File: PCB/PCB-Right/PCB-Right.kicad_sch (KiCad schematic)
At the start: 56 parts, among them J1 USB_C_Receptacle_USB2.0_16P, J2 Conn_ARM_JTAG_SWD_10, Q1 2N7002, SW1 SW_RST, SW2 SW_SPDT, U2 XC6206PxxxMR, U3 SRV05-4, U4 BQ24075RGT, U5 MDBT50Q-1MV2, Y1 32.768KHz

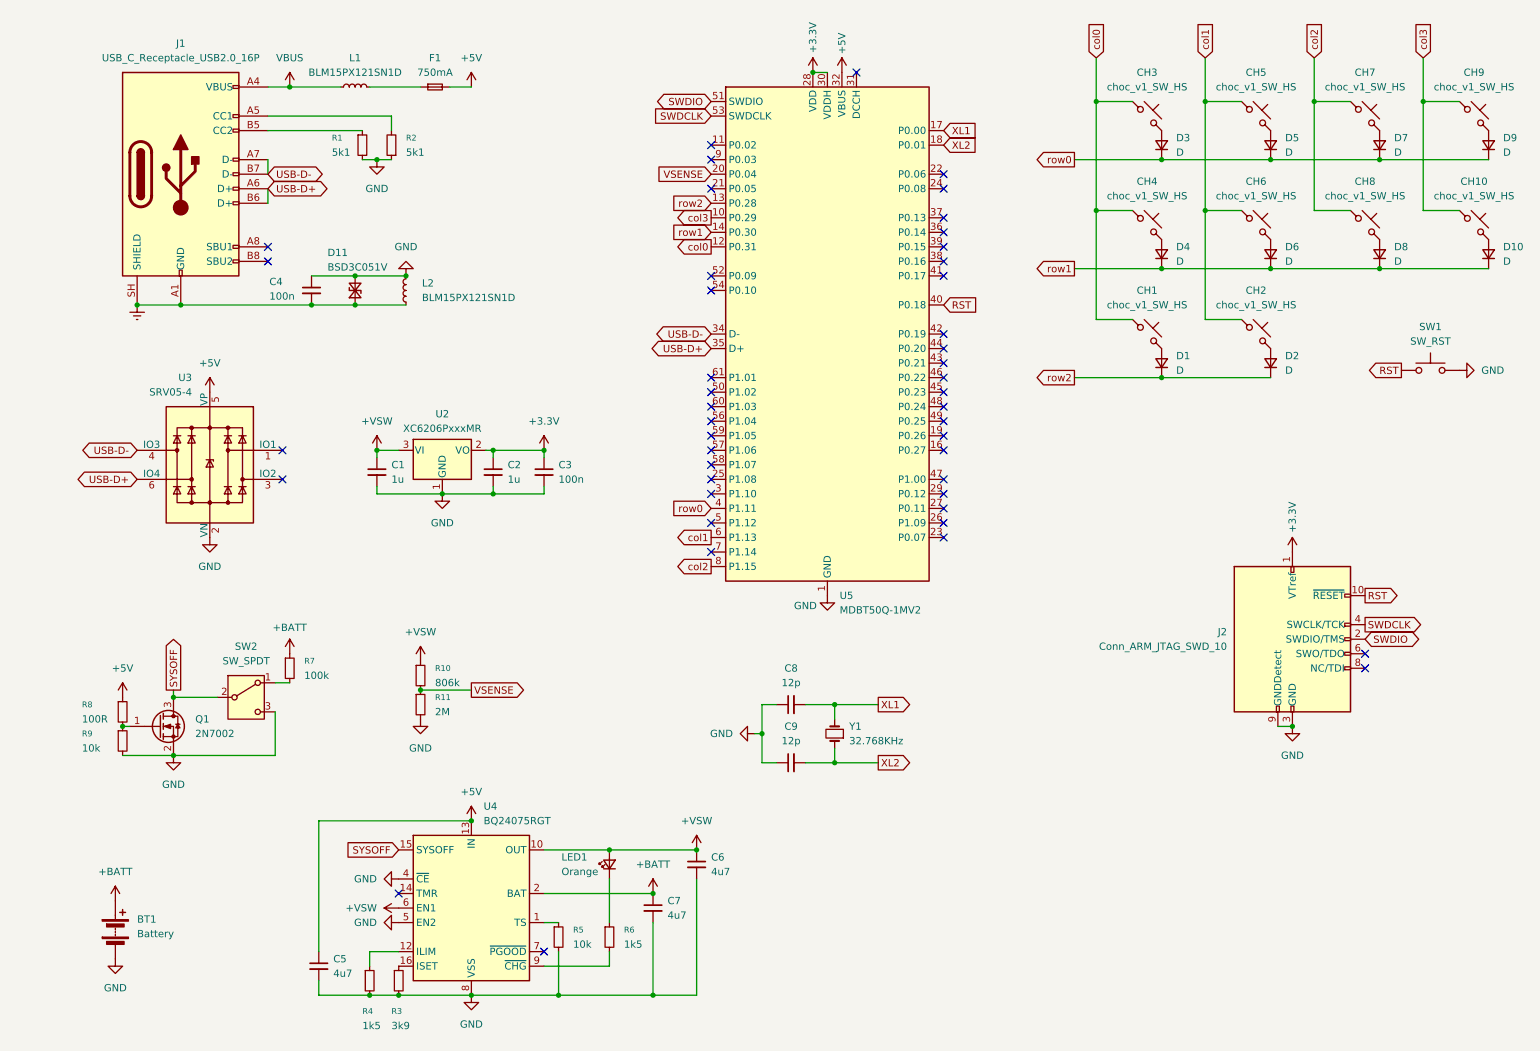
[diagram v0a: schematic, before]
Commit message: replace voltage regulator with DCCH inductor
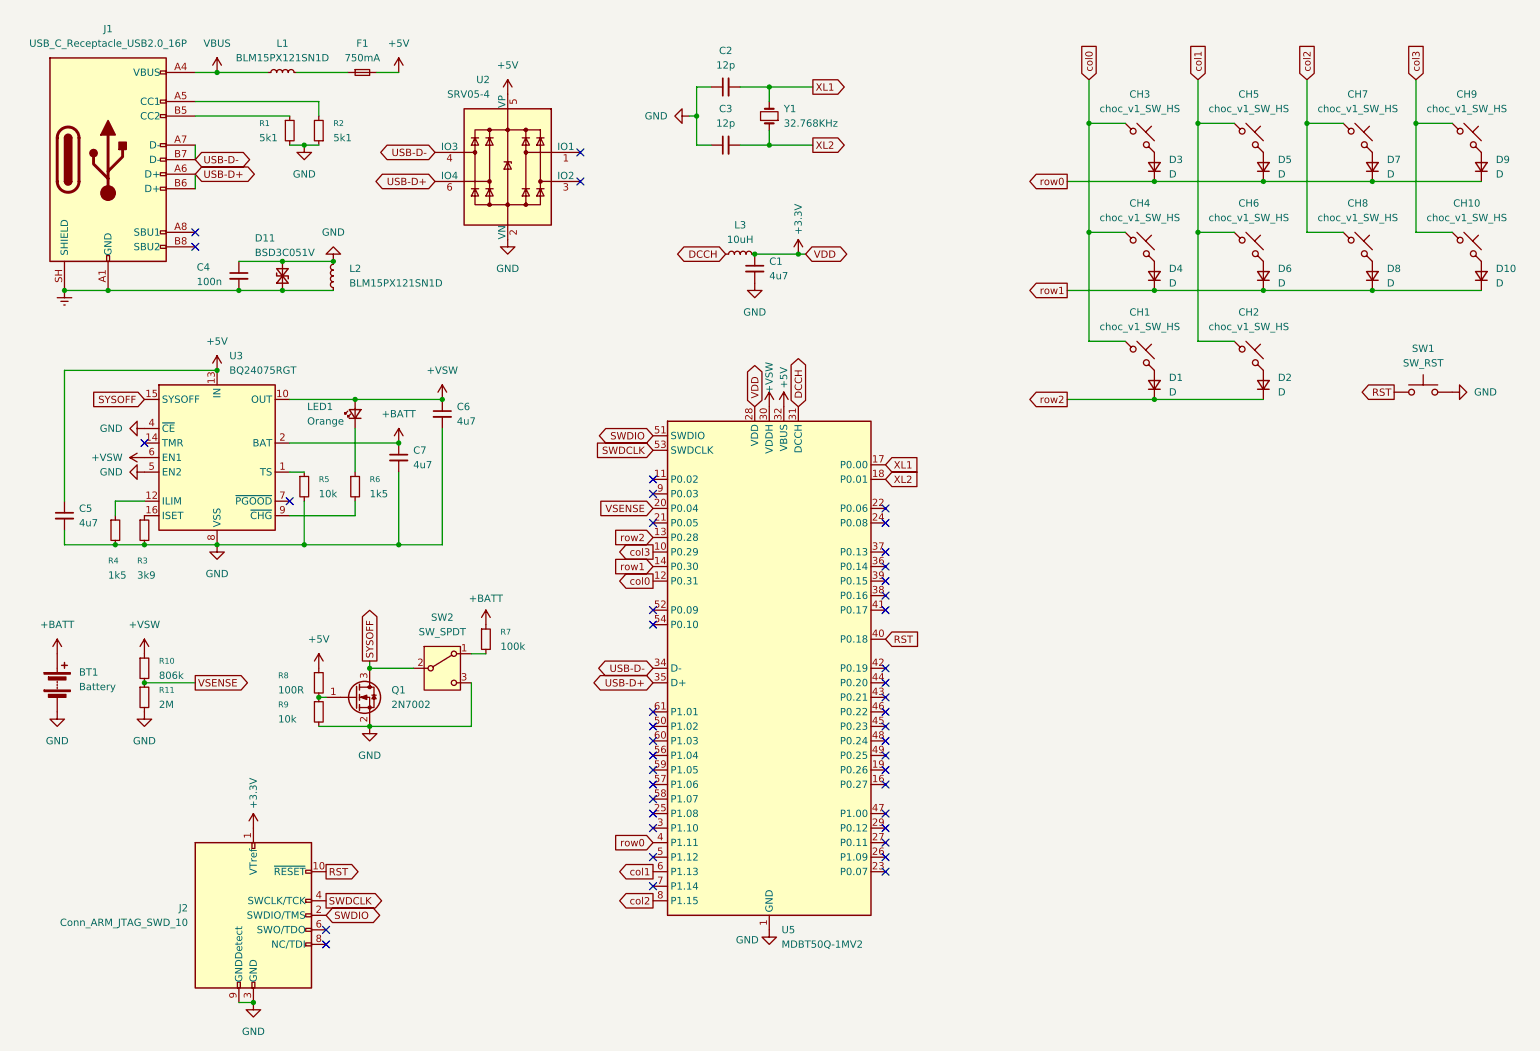
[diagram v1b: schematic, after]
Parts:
- removed C2: 1u, Capacitor_SMD:C_0603_1608Metric, symbol Device:C_Small
- removed C3: 100n, Capacitor_SMD:C_0603_1608Metric, symbol Device:C_Small
- removed U2: XC6206PxxxMR, Package_TO_SOT_SMD:SOT-23-3, symbol Regulator_Linear:XC6206PxxxMR
- added L3: 10uH, Inductor_SMD:L_0603_1608Metric, symbol Device:L_Small
- C1: value 1u -> 4u7
- renumbered C8 to C2, C9 to C3, U3 to U2, U4 to U3
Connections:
- net +3.3V: now also C1.1, L3.2; no longer U5.30 (VDDH)
- net +VSW: now also U5.30 (VDDH); no longer C1.1
- net DCCH: now reaches U5.31 (DCCH)
- net DCCH: now also L3.1
- no-connect marks 46 -> 45
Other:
- moved on the sheet: BT1, C1, C2, C3, C4, C5, C6, C7, CH1, CH10, CH2, CH3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

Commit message: remove backup and lock files
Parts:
- renumbered U5 to U1
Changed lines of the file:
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@@
 	)
 	(global_label "VDD"
-		(shape bidirectional)
+		(shape output)
 		(at 144.78 85.09 90)
 		(fields_autoplaced yes)
@@
 		)
 		(property "Intersheetrefs" "${INTERSHEET_REFS}"
-			(at 144.78 77.3649 90)
+			(at 144.78 78.4762 90)
 			(hide yes)
 			(show_name no)
@@
 	)
 	(global_label "VDD"
-		(shape bidirectional)
+		(shape input)
 		(at 153.67 58.42 0)
 		(fields_autoplaced yes)
@@
 		)
 		(property "Intersheetrefs" "${INTERSHEET_REFS}"
-			(at 161.3951 58.42 0)
+			(at 160.2838 58.42 0)
 			(hide yes)
 			(show_name no)
@@
 	)
 	(global_label "DCCH"
-		(shape bidirectional)
+		(shape input)
 		(at 139.7 58.42 180)
 		(fields_autoplaced yes)
@@
 		)
 		(property "Intersheetrefs" "${INTERSHEET_REFS}"
-			(at 130.463 58.42 0)
+			(at 131.5743 58.42 0)
 			(hide yes)
 			(show_name no)
@@
 	)
 	(global_label "DCCH"
-		(shape bidirectional)
+		(shape output)
 		(at 152.4 85.09 90)
 		(fields_autoplaced yes)
@@
 		)
 		(property "Intersheetrefs" "${INTERSHEET_REFS}"
-			(at 152.4 75.853 90)
+			(at 152.4 76.9643 90)
 			(hide yes)
 			(show_name no)
@@
 		(dnp no)
 		(fields_autoplaced yes)
-		(property "Reference" "U5"
+		(property "Reference" "U1"
 			(at 149.4633 176.53 0)
 			(show_name no)
@@
 			(project "PCB-Right"
 				(path "/d27bf40e-f12c-4fc4-af83-8c0622ff945a"
-					(reference "U5")
+					(reference "U1")
 					(unit 1)
 				)
